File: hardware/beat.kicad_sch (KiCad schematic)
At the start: 43 parts, among them J101 Cortex, J102 DX07S016JA3, J103 1x08, SW101 SKSG, SW102 SKSG, U101 TPS78433QWDRBRQ1, U102 ATSAMD51G, Y101 32k768

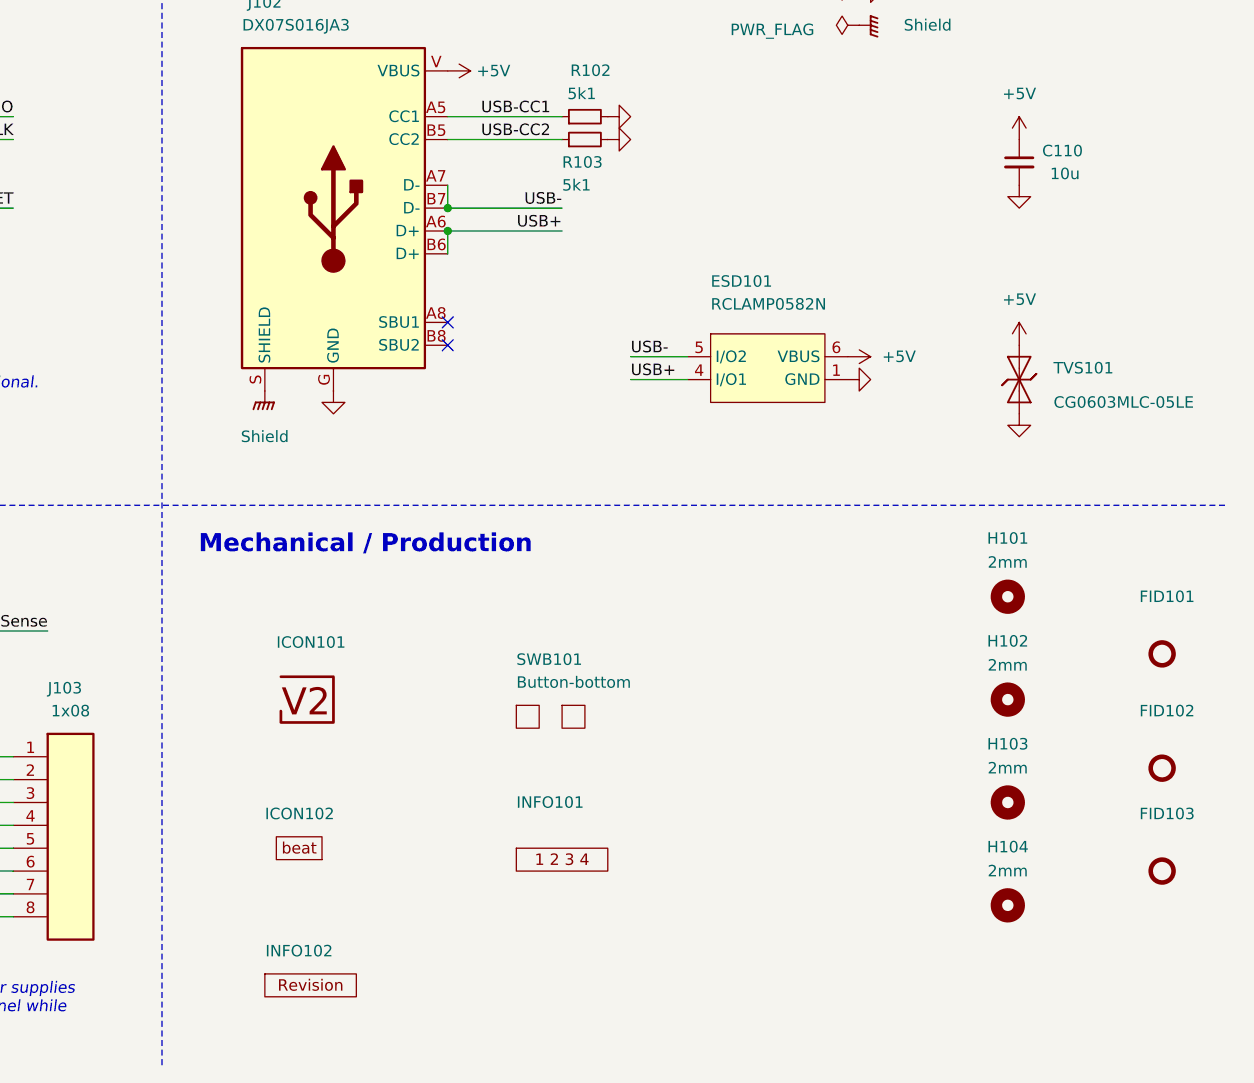
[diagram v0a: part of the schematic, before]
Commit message: Replace diode
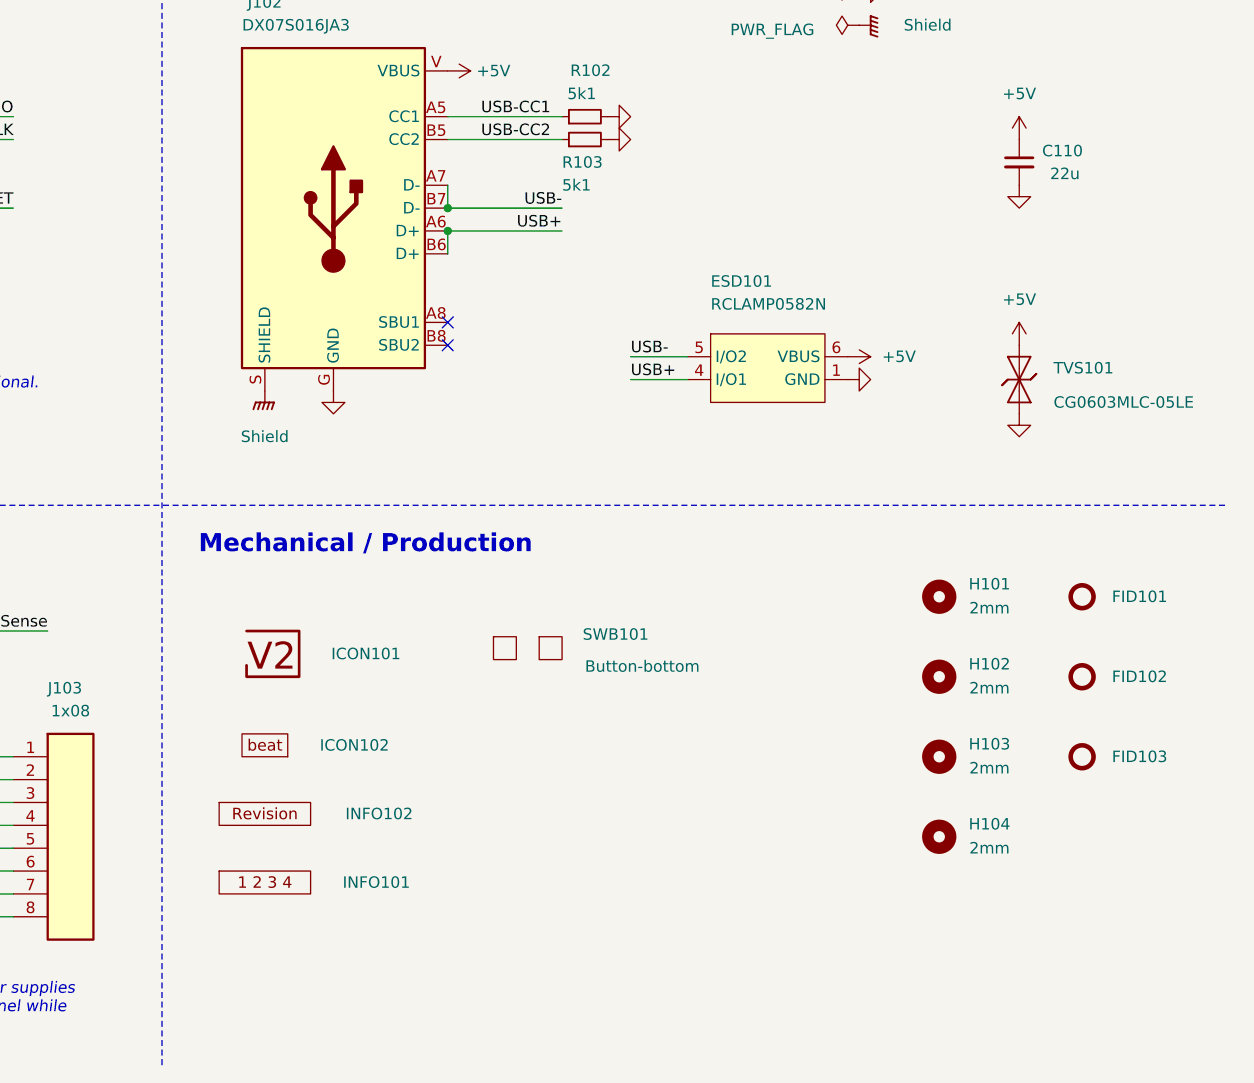
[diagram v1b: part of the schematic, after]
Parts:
- C108, C109: Manufacturer YAGEO -> TDK; Mouser 603-CC603JRNPO9BN180 -> 810-CGA3E2C0G1H180J; Product CC0603JRNPO9BN180 -> CGA3E2C0G1H180J080AA
- C110: value 10u -> 22u
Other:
- moved on the sheet: FID101, FID102, FID103, H101, H102, H103, H104, ICON101, ICON102, INFO101, INFO102, SWB101

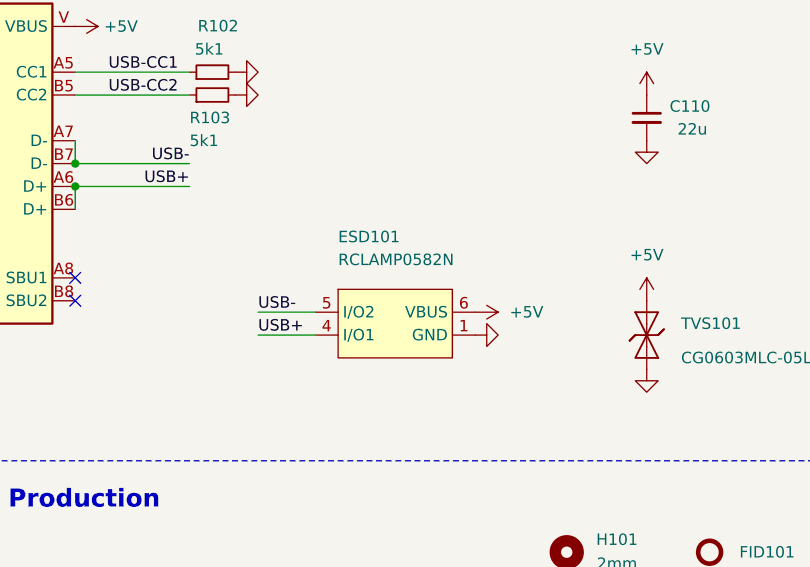
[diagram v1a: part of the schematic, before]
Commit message: Update ESD suppressor
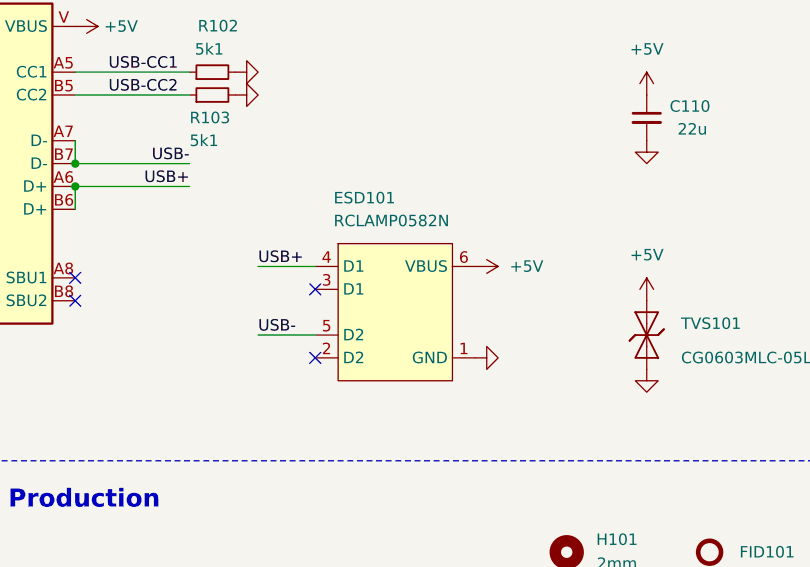
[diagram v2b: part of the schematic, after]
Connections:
- no-connect marks 23 -> 25
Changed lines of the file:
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@@
 	(title_block
 		(title "V2 beat")
-		(date "2026-03-11")
+		(date "2026-03-14")
 		(rev "2026-03-11")
 		(company "Versio Duo")
@@
 	)
 	(no_connect
+		(at 224.79 115.57)
+	)
+	(no_connect
 		(at 72.39 33.02)
 	)
 	(no_connect
+		(at 224.79 123.19)
+	)
+	(no_connect
 		(at 60.96 83.82)
 	)
@@
 	(wire
 		(pts
-			(xy 218.44 118.11) (xy 224.79 118.11)
+			(xy 218.44 120.65) (xy 224.79 120.65)
 		)
 		(stroke
@@
 	(wire
 		(pts
-			(xy 40.64 101.6) (xy 60.96 101.6)
+			(xy 218.44 113.03) (xy 224.79 113.03)
 		)
 		(stroke
@@
 	(wire
 		(pts
-			(xy 64.77 185.42) (xy 77.47 185.42)
+			(xy 40.64 101.6) (xy 60.96 101.6)
 		)
 		(stroke
@@
 	(wire
 		(pts
-			(xy 218.44 120.65) (xy 224.79 120.65)
+			(xy 64.77 185.42) (xy 77.47 185.42)
 		)
 		(stroke
@@
 	)
 	(label "USB+"
+		(at 218.44 113.03 0)
+		(effects
+			(font
+				(size 1.27 1.27)
+			)
+			(justify left bottom)
+		)
+	)
+	(label "USB+"
 		(at 210.82 104.14 180)
 		(effects
@@
 		)
 	)
-	(label "USB+"
-		(at 218.44 120.65 0)
-		(effects
-			(font
-				(size 1.27 1.27)
-			)
-			(justify left bottom)
-		)
-	)
 	(label "Button-LED"
 		(at 110.49 190.5 180)
@@
 	)
 	(label "USB-"
-		(at 218.44 118.11 0)
+		(at 218.44 120.65 0)
 		(effects
 			(font
@@
 		(dnp no)
 		(property "Reference" "ESD101"
-			(at 227.33 110.49 0)
+			(at 226.822 106.172 0)
 			(effects
 				(font
@@
 		)
 		(property "Value" "RCLAMP0582N"
-			(at 227.33 113.03 0)
+			(at 226.822 108.712 0)
 			(effects
 				(font
@@
 	(symbol
 		(lib_id "V2_power:+5V")
-		(at 242.57 118.11 270)
+		(at 242.57 113.03 270)
 		(unit 1)
 		(exclude_from_sim no)
@@
 		(dnp no)
 		(property "Reference" "#PWR127"
-			(at 238.76 118.11 0)
+			(at 238.76 113.03 0)
 			(effects
 				(font
@@
 		)
 		(property "Value" "+5V"
-			(at 246.38 118.11 90)
+			(at 246.38 113.03 90)
 			(effects
 				(font
@@
 		)
 		(property "Footprint" ""
-			(at 242.57 118.11 0)
+			(at 242.57 113.03 0)
 			(effects
 				(font
@@
 		)
 		(property "Datasheet" ""
-			(at 242.57 118.11 0)
+			(at 242.57 113.03 0)
 			(effects
 				(font
@@
 		)
 		(property "Description" ""
-			(at 242.57 118.11 0)
+			(at 242.57 113.03 0)
 			(effects
 				(font
@@
 		(at 156.21 170.18 0)
 		(unit 1)
-		(exclude_from_sim yes)
+		(exclude_from_sim no)
 		(in_bom yes)
 		(on_board yes)
@@
 			)
 		)
+		(property "Sim.Enable" "0"
+			(at 156.21 170.18 0)
+			(effects
+				(font
+					(size 1.27 1.27)
+				)
+				(hide yes)
+			)
+		)
 		(pin "1"
 		)
@@
 		(at 207.01 150.495 0)
 		(unit 1)
-		(exclude_from_sim yes)
+		(exclude_from_sim no)
 		(in_bom no)
 		(on_board yes)
@@
 			)
 		)
+		(property "Sim.Enable" "0"
+			(at 207.01 150.495 0)
+			(effects
+				(font
+					(size 1.27 1.27)
+				)
+				(hide yes)
+			)
+		)
 		(instances
 			(project "beat"
@@
 		(at 177.8 161.29 0)
 		(unit 1)
-		(exclude_from_sim yes)
+		(exclude_from_sim no)
 		(in_bom no)
 		(on_board yes)
@@
 			)
 		)
+		(property "Sim.Enable" "0"
+			(at 177.8 161.29 0)
+			(effects
+				(font
+					(size 1.27 1.27)
+				)
+				(hide yes)
+			)
+		)
 		(instances
 			(project "beat"
@@
 	(symbol
 		(lib_id "V2_power:GND")
-		(at 242.57 120.65 90)
+		(at 242.57 123.19 90)
 		(unit 1)
 		(exclude_from_sim no)
@@
 		(dnp no)
 		(property "Reference" "#PWR128"
-			(at 248.92 120.65 0)
+			(at 248.92 123.19 0)
 			(effects
 				(font
@@
 		)
 		(property "Value" "GND"
-			(at 246.38 120.65 90)
+			(at 246.38 123.19 90)
 			(effects
 				(font
@@
 		)
 		(property "Footprint" ""
-			(at 242.57 120.65 0)
+			(at 242.57 123.19 0)
 			(effects
 				(font
@@
 		)
 		(property "Datasheet" ""
-			(at 242.57 120.65 0)
+			(at 242.57 123.19 0)
 			(effects
 				(font
@@
 		)
 		(property "Description" ""
-			(at 242.57 120.65 0)
+			(at 242.57 123.19 0)
 			(effects
 				(font

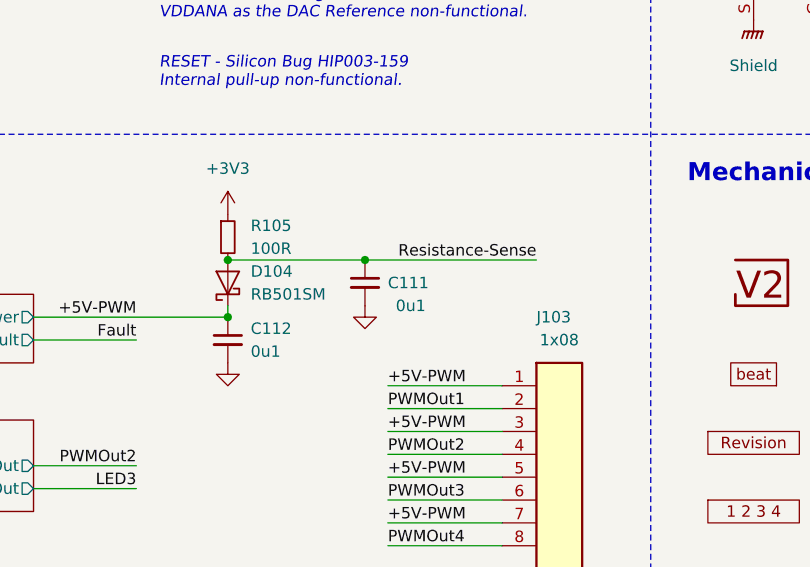
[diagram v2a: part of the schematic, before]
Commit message: Replace diode
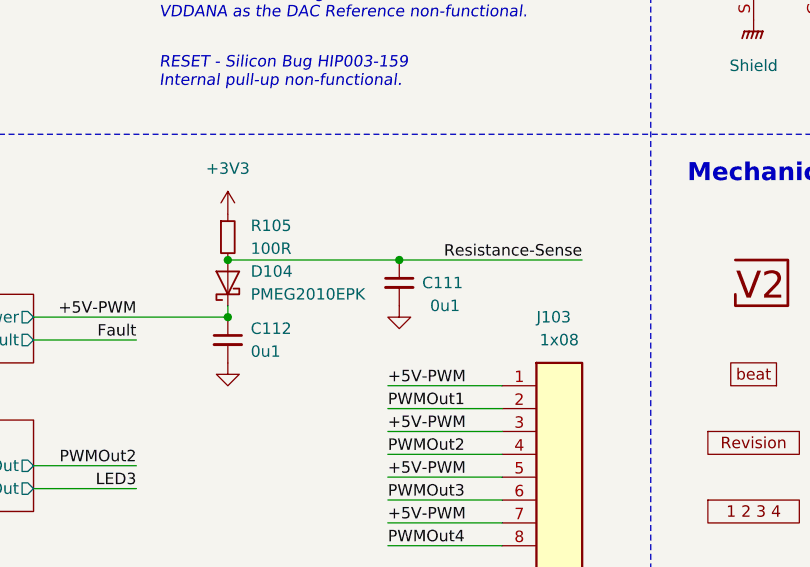
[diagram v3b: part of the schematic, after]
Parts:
- C108, C109: Rating (none) -> 50V
- D104: value RB501SM -> PMEG2010EPK; footprint V2_Diode_SMD:D_SOD-523 -> V2_Diode_SMD:D_SOD-1608; symbol V2_Diode:RB501SM -> V2_Diode:PMEG2010EPK; Manufacturer ROHM Semiconductor -> Nexperia; Mouser 755-RB501SM-30FHT2R -> 771-PMEG2010EPK; Product RB501SM-30FHT2R -> PMEG2010EPK; Rating (none) -> 20V
- INFO102: value ~ -> (none)
- SW101, SW102: Rating (none) -> 1.6N
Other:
- moved on the sheet: C111

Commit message: Update
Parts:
- C101: renamed from C108; Id (none) -> Capacitor:${SYMBOL_NAME}
- C102: renamed from C109; Id (none) -> Capacitor:${SYMBOL_NAME}
- C103: renamed from C101; Id (none) -> Capacitor:${SYMBOL_NAME}
- C104: renamed from C102; Id (none) -> Capacitor:${SYMBOL_NAME}
- C105: renamed from C103; Id (none) -> Capacitor:${SYMBOL_NAME}
- C106: renamed from C104; Id (none) -> Capacitor:${SYMBOL_NAME}
- C107: renamed from C105; Id (none) -> Capacitor:${SYMBOL_NAME}
- C108: renamed from C112; Id (none) -> Capacitor:${SYMBOL_NAME}
- C109: renamed from C111; Id (none) -> Capacitor:${SYMBOL_NAME}
- C110: renamed from C106; Id (none) -> Capacitor:${SYMBOL_NAME}
- C111: renamed from C107; Id (none) -> Capacitor:${SYMBOL_NAME}
- C112: renamed from C110; Id (none) -> Capacitor:${SYMBOL_NAME}
- D101: renamed from D104; Id (none) -> Diode:${SYMBOL_NAME}
- D102: renamed from D103; Id (none) -> LED:${SYMBOL_NAME}; Rating (none) -> 605nm
- D103: renamed from D101; Id (none) -> LED:${SYMBOL_NAME}; Rating (none) -> 15mA
- D104: renamed from D102; Id (none) -> LED:${SYMBOL_NAME}; Rating (none) -> 15mA
- ESD101: Id (none) -> ESD:${SYMBOL_NAME}; Rating (none) -> 20kV
- J102: renamed from J103; Id (none) -> Header:${SYMBOL_NAME}
- J103: renamed from J102; Id (none) -> USB:${SYMBOL_NAME}; Rating (none) -> USB2.0
- R101: renamed from R104; Id (none) -> Resistor:${SYMBOL_NAME}
- R102: renamed from R105; Id (none) -> Resistor:${SYMBOL_NAME}
- R103: renamed from R101; Id (none) -> Resistor:${SYMBOL_NAME}
- R104: renamed from R102; Id (none) -> Resistor:${SYMBOL_NAME}
- R105: renamed from R103; Id (none) -> Resistor:${SYMBOL_NAME}
- SW101: renamed from SW102; Id (none) -> Button:${SYMBOL_NAME}
- SW102: renamed from SW101; Id (none) -> Button:${SYMBOL_NAME}
- TVS101: Id (none) -> Diode:${SYMBOL_NAME}
- U101: renamed from U102; Id (none) -> MCU:${SYMBOL_NAME}; Rating (none) -> Cortex-M4F
- U102: renamed from U101; Id (none) -> LDO:${SYMBOL_NAME}; Rating (none) -> 300mA
- Y101: Id (none) -> Crystal:${SYMBOL_NAME}; Rating (none) -> 10ppm
- renumbered ICON102 to ICON101, ICON101 to ICON102, INFO102 to INFO101, INFO101 to INFO102
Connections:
- net VDDCORE renamed +VCORE

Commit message: Good Bye Imperial
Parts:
- C101, C102: footprint V2_Capacitor_SMD:C_0603 -> V2_Capacitor_SMD:C_1608; symbol V2_Capacitor:0603_18p -> V2_Capacitor:1608_18p
- C103: footprint V2_Capacitor_SMD:C_0603 -> V2_Capacitor_SMD:C_1608; symbol V2_Capacitor:0603_10u -> V2_Capacitor:1608_10u
- C104, C105, C106, C107, C108, C109: footprint V2_Capacitor_SMD:C_0603 -> V2_Capacitor_SMD:C_1608; symbol V2_Capacitor:0603_0u1 -> V2_Capacitor:1608_0u1
- C110, C111: footprint V2_Capacitor_SMD:C_0805 -> V2_Capacitor_SMD:C_2012; symbol V2_Capacitor:0805_10u -> V2_Capacitor:2012_10u
- C112: footprint V2_Capacitor_SMD:C_1210 -> V2_Capacitor_SMD:C_3225; symbol V2_Capacitor:1210_22u -> V2_Capacitor:3225_22u
- D102: symbol V2_LED:0603_Orange -> V2_LED:1608_Orange
- R101: footprint V2_Resistor_SMD:R_0603 -> V2_Resistor_SMD:R_1608; symbol V2_Resistor:0603_100k -> V2_Resistor:1608_100k
- R102: footprint V2_Resistor_SMD:R_0603 -> V2_Resistor_SMD:R_1608; symbol V2_Resistor:0603_100R -> V2_Resistor:1608_100R
- R103: footprint V2_Resistor_SMD:R_0603 -> V2_Resistor_SMD:R_1608; symbol V2_Resistor:0603_330R -> V2_Resistor:1608_330R
- R104, R105: footprint V2_Resistor_SMD:R_0603 -> V2_Resistor_SMD:R_1608; symbol V2_Resistor:0603_5k1 -> V2_Resistor:1608_5k1
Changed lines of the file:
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@@
 	)
 	(symbol
-		(lib_id "V2_Capacitor:0603_0u1")
+		(lib_id "V2_Capacitor:1608_0u1")
 		(at 116.84 24.13 0)
 		(unit 1)
@@
 			)
 		)
-		(property "Footprint" "V2_Capacitor_SMD:C_0603"
+		(property "Footprint" "V2_Capacitor_SMD:C_1608"
 			(at 116.84 41.148 0)
 			(hide yes)
@@
 	)
 	(symbol
-		(lib_id "V2_Capacitor:0603_0u1")
+		(lib_id "V2_Capacitor:1608_0u1")
 		(at 119.38 157.48 0)
 		(unit 1)
@@
 			)
 		)
-		(property "Footprint" "V2_Capacitor_SMD:C_0603"
+		(property "Footprint" "V2_Capacitor_SMD:C_1608"
 			(at 119.38 174.498 0)
 			(hide yes)
@@
 	)
 	(symbol
-		(lib_id "V2_LED:0603_Orange")
+		(lib_id "V2_LED:1608_Orange")
 		(at 127 55.88 0)
 		(mirror y)
@@
 	)
 	(symbol
-		(lib_id "V2_Capacitor:0805_10u")
+		(lib_id "V2_Capacitor:2012_10u")
 		(at 205.74 39.37 0)
 		(unit 1)
@@
 			)
 		)
-		(property "Footprint" "V2_Capacitor_SMD:C_0805"
+		(property "Footprint" "V2_Capacitor_SMD:C_2012"
 			(at 205.74 56.388 0)
 			(hide yes)
@@
 	)
 	(symbol
-		(lib_id "V2_Resistor:0603_100R")
+		(lib_id "V2_Resistor:1608_100R")
 		(at 119.38 146.05 0)
 		(unit 1)
@@
 			)
 		)
-		(property "Footprint" "V2_Resistor_SMD:R_0603"
+		(property "Footprint" "V2_Resistor_SMD:R_1608"
 			(at 119.38 161.798 0)
 			(hide yes)
@@
 	)
 	(symbol
-		(lib_id "V2_Resistor:0603_5k1")
+		(lib_id "V2_Resistor:1608_5k1")
 		(at 213.36 91.44 90)
 		(unit 1)
@@
 			)
 		)
-		(property "Footprint" "V2_Resistor_SMD:R_0603"
+		(property "Footprint" "V2_Resistor_SMD:R_1608"
 			(at 229.108 91.44 0)
 			(hide yes)
@@
 	)
 	(symbol
-		(lib_id "V2_Capacitor:0805_10u")
+		(lib_id "V2_Capacitor:2012_10u")
 		(at 179.07 39.37 0)
 		(unit 1)
@@
 			)
 		)
-		(property "Footprint" "V2_Capacitor_SMD:C_0805"
+		(property "Footprint" "V2_Capacitor_SMD:C_2012"
 			(at 179.07 56.388 0)
 			(hide yes)
@@
 	)
 	(symbol
-		(lib_id "V2_Capacitor:0603_18p")
+		(lib_id "V2_Capacitor:1608_18p")
 		(at 33.02 46.99 0)
 		(unit 1)
@@
 			)
 		)
-		(property "Footprint" "V2_Capacitor_SMD:C_0603"
+		(property "Footprint" "V2_Capacitor_SMD:C_1608"
 			(at 33.02 64.008 0)
 			(hide yes)
@@
 	)
 	(symbol
-		(lib_id "V2_Capacitor:0603_10u")
+		(lib_id "V2_Capacitor:1608_10u")
 		(at 66.04 24.13 0)
 		(unit 1)
@@
 			)
 		)
-		(property "Footprint" "V2_Capacitor_SMD:C_0603"
+		(property "Footprint" "V2_Capacitor_SMD:C_1608"
 			(at 66.04 41.148 0)
 			(hide yes)
@@
 	)
 	(symbol
-		(lib_id "V2_Capacitor:0603_0u1")
+		(lib_id "V2_Capacitor:1608_0u1")
 		(at 138.43 151.13 0)
 		(unit 1)
@@
 			)
 		)
-		(property "Footprint" "V2_Capacitor_SMD:C_0603"
+		(property "Footprint" "V2_Capacitor_SMD:C_1608"
 			(at 138.43 168.148 0)
 			(hide yes)
@@
 	)
 	(symbol
-		(lib_id "V2_Capacitor:0603_18p")
+		(lib_id "V2_Capacitor:1608_18p")
 		(at 27.94 46.99 0)
 		(unit 1)
@@
 			)
 		)
-		(property "Footprint" "V2_Capacitor_SMD:C_0603"
+		(property "Footprint" "V2_Capacitor_SMD:C_1608"
 			(at 27.94 64.008 0)
 			(hide yes)
@@
 	)
 	(symbol
-		(lib_id "V2_Resistor:0603_330R")
+		(lib_id "V2_Resistor:1608_330R")
 		(at 137.16 55.88 90)
 		(unit 1)
@@
 			)
 		)
-		(property "Footprint" "V2_Resistor_SMD:R_0603"
+		(property "Footprint" "V2_Resistor_SMD:R_1608"
 			(at 152.908 55.88 0)
 			(hide yes)
@@
 	)
 	(symbol
-		(lib_id "V2_Capacitor:1210_22u")
+		(lib_id "V2_Capacitor:3225_22u")
 		(at 261.62 96.52 0)
 		(unit 1)
@@
 			)
 		)
-		(property "Footprint" "V2_Capacitor_SMD:C_1210"
+		(property "Footprint" "V2_Capacitor_SMD:C_3225"
 			(at 261.62 113.538 0)
 			(hide yes)
@@
 	)
 	(symbol
-		(lib_id "V2_Capacitor:0603_0u1")
+		(lib_id "V2_Capacitor:1608_0u1")
 		(at 106.68 24.13 0)
 		(unit 1)
@@
 			)
 		)
-		(property "Footprint" "V2_Capacitor_SMD:C_0603"
+		(property "Footprint" "V2_Capacitor_SMD:C_1608"
 			(at 106.68 41.148 0)
 			(hide yes)
@@
 	)
 	(symbol
-		(lib_id "V2_Capacitor:0603_0u1")
+		(lib_id "V2_Capacitor:1608_0u1")
 		(at 86.36 24.13 0)
 		(unit 1)
@@
 			)
 		)
-		(property "Footprint" "V2_Capacitor_SMD:C_0603"
+		(property "Footprint" "V2_Capacitor_SMD:C_1608"
 			(at 86.36 41.148 0)
 			(hide yes)
@@
 	)
 	(symbol
-		(lib_id "V2_Capacitor:0603_0u1")
+		(lib_id "V2_Capacitor:1608_0u1")
 		(at 96.52 24.13 0)
 		(unit 1)
@@
 			)
 		)
-		(property "Footprint" "V2_Capacitor_SMD:C_0603"
+		(property "Footprint" "V2_Capacitor_SMD:C_1608"
 			(at 96.52 41.148 0)
 			(hide yes)
@@
 	)
 	(symbol
-		(lib_id "V2_Resistor:0603_5k1")
+		(lib_id "V2_Resistor:1608_5k1")
 		(at 213.36 93.98 90)
 		(unit 1)
@@
 			)
 		)
-		(property "Footprint" "V2_Resistor_SMD:R_0603"
+		(property "Footprint" "V2_Resistor_SMD:R_1608"
 			(at 229.108 93.98 0)
 			(hide yes)
@@
 	)
 	(symbol
-		(lib_id "V2_Resistor:0603_100k")
+		(lib_id "V2_Resistor:1608_100k")
 		(at 58.42 121.92 90)
 		(unit 1)
@@
 			)
 		)
-		(property "Footprint" "V2_Resistor_SMD:R_0603"
+		(property "Footprint" "V2_Resistor_SMD:R_1608"
 			(at 74.168 121.92 0)
 			(hide yes)
